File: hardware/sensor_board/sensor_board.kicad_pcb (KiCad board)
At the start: 4 copper layers, 50 x 34 mm, 64 parts, among them J1 CORTEX-SWD-6, J2 Conn_01x04_MountingPin, J3 Conn_01x10_MountingPin, Q1 SI2337DS-T1-BE3, Q2 SI2337DS-T1-BE3, Q3 BSH203,215, U1 ATSAMC21E17A, U2 TCAN332G, U3 NCP718xSN330, U4 LMZM23600V5, U5 SHT30-DIS, U6 BMP384, U7 SCD4x, U8 SGP30, U9 BH1751FVI, Y1 Resonator

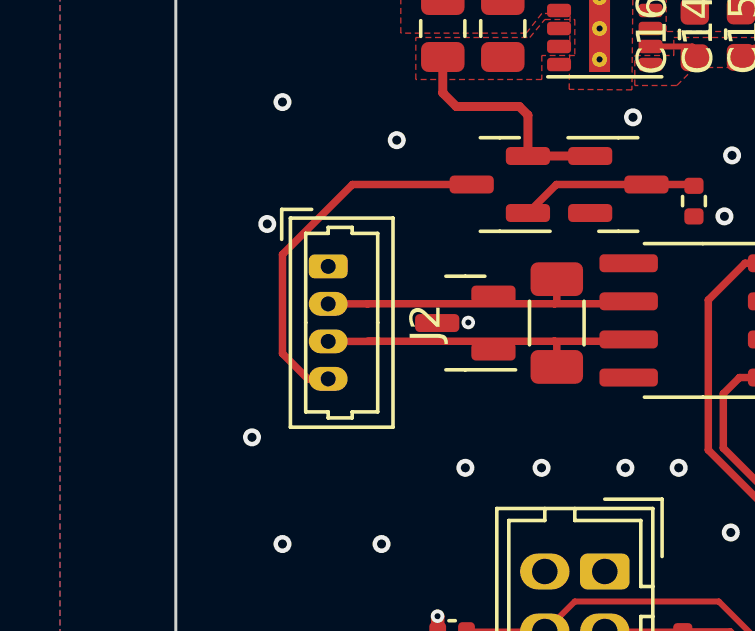
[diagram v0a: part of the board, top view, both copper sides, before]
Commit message: updated board with new connector
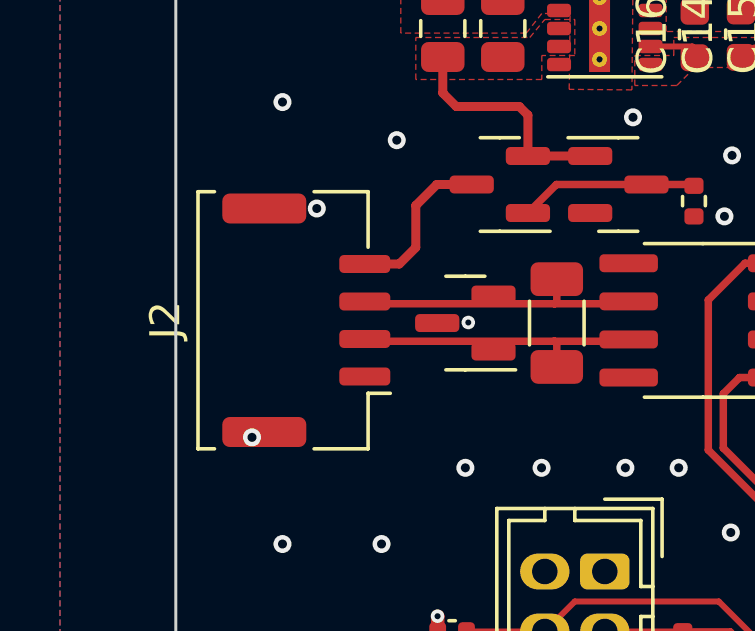
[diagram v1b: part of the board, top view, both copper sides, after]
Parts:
- J2: footprint Connector_Molex:Molex_PicoBlade_53047-0410_1x04_P1.25mm_Vertical -> Connector_Molex:Molex_CLIK-Mate_502382-0470_1x04-1MP_P1.25mm_Vertical
- moved J2 1.94 mm to (4.35, 16.9), turned to 90 degrees
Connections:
- J2 pad 2: /CAN- -> /CAN+
- J2 pad 3: /CAN+ -> /CAN-
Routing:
- net Net-(J2-Pad4): track 12.4 -> 5.48 mm
- net /CAN+: track 11.3 -> 9.61 mm
- net /CAN-: track 10.9 -> 9.58 mm

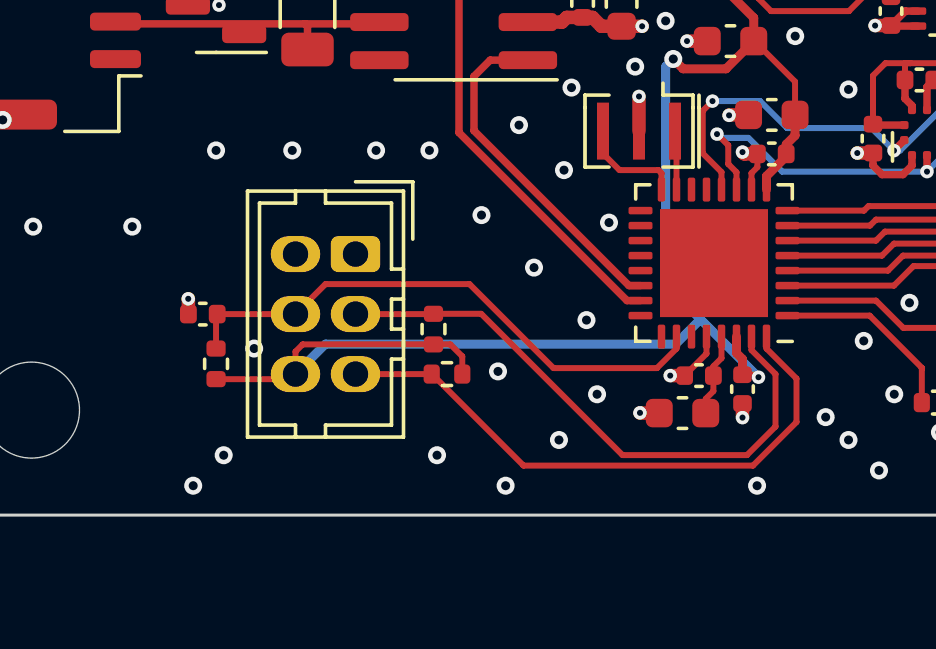
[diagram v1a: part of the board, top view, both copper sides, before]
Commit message: changed to tag connect due to chip shortage
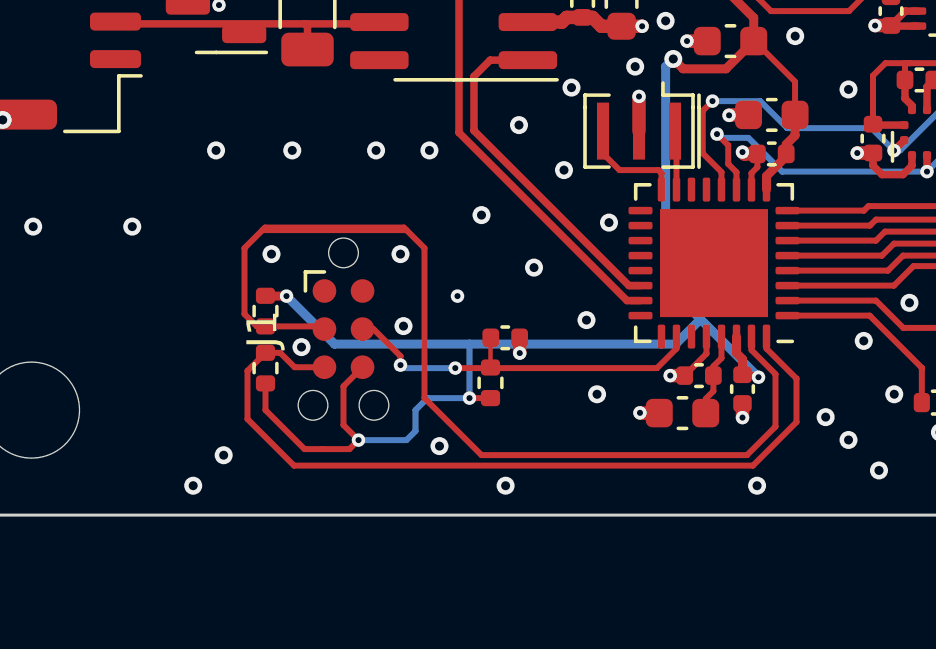
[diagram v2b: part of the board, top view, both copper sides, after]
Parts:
- J1: footprint Connector_Hirose:Hirose_DF11-6DP-2DSA_2x03_P2.00mm_Vertical -> Connector:Tag-Connect_TC2030-IDC-NL_2x03_P1.27mm_Vertical
- moved C1 10.1 mm to (19.3, 28.1), turned to 180 degrees
- moved R1 9.17 mm to (18.8, 29.6)
- moved R3 6.05 mm to (11.3, 29.1), turned to 90 degrees
- moved R2 5.63 mm to (11.3, 27.2), turned to -90 degrees
- moved J1 2.53 mm to (13.9, 27.8)
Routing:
- net /SWCLK: track 20.0 -> 38.0 mm
- net /SWDIO: track 19.8 -> 27.4 mm
- net VDD: track 98.9 -> 105.0 mm, vias 4 -> 7
- net ~{RESET}: track 18.7 -> 13.0 mm, vias 0 -> 2
- net GND: vias 102 -> 104

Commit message: some stuff!
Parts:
- added C12: 1uF / 10V, Capacitor_SMD:C_0603_1608Metric, F.Cu at (17.5, 3.34)
- added C14: 100nF / 6.3V, Capacitor_SMD:C_0402_1005Metric, F.Cu at (24.3, 3.03)
- C13: renamed from C12; value 1uF / 10V -> 100nF / 10V; footprint Capacitor_SMD:C_0603_1608Metric -> Capacitor_SMD:C_0402_1005Metric
- moved R2 11.2 mm to (22.1, 29.9), turned to 180 degrees
- moved R3 10.8 mm to (22.1, 28.8), turned to 180 degrees
- moved J1 5.31 mm to (19.1, 28.6)
- moved R1 3.19 mm to (16.6, 27.3), turned to -90 degrees
- moved C1 2.89 mm to (16.6, 29.2), turned to 90 degrees
- moved C15 0.99 mm to (25.6, 3.32)
- moved C24 0.18 mm to (38.7, 7.67)
- renumbered C13 to C15, C14 to C16, C15 to C17, C16 to C18, C17 to C19, C18 to C20, C19 to C21, C20 to C22, C21 to C23, C22 to C24, C23 to C25, C24 to C26, C25 to C27, C26 to C28, REF** to Hole1, REF** to Hole2, REF** to Hole3, REF** to Hole4
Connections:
- J1 pad 1: unconnected-(J1-Pad1) -> VDD
- J1 pad 2: GND -> /SWDIO
- J1 pad 3: /SWCLK -> ~{RESET}
- J1 pad 4: ~{RESET} -> /SWCLK
- J1 pad 5: /SWDIO -> GND
- J1 pad 6: VDD -> unconnected-(J1-Pad6)
- U1 pad 22: /CAN_{TX} -> unconnected-(U1-Pad22)
- U1 pad 23: /CAN_{RX} -> /CAN_{TX}
- U1 pad 24: unconnected-(U1-Pad24) -> /CAN_{RX}
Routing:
- net /SWCLK: track 38.0 -> 13.3 mm
- net /SWDIO: track 27.4 -> 12.5 mm, vias 0 -> 2
- net VDD: track 105.0 -> 94.5 mm, vias 7 -> 4
- net +5V: track 53.5 -> 55.5 mm
- net ~{RESET}: track 13.0 -> 14.8 mm
- net /VDDSW: track 110.4 -> 109.4 mm
- net /CAN_{RX}: track 16.2 -> 17.0 mm
- net /CAN_{TX}: track 11.5 -> 12.4 mm
- net GND: track 38.7 -> 37.9 mm, vias 104 -> 102
